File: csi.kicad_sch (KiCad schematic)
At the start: 40 parts, among them J15 Bus_DDR4_SODIMM_CUSTOM_Jetson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, T8 BSS138PW, U10 TPS7A0528PDBVR, U11 TLV75512PDBVR, U4 PCA9547_VQFN

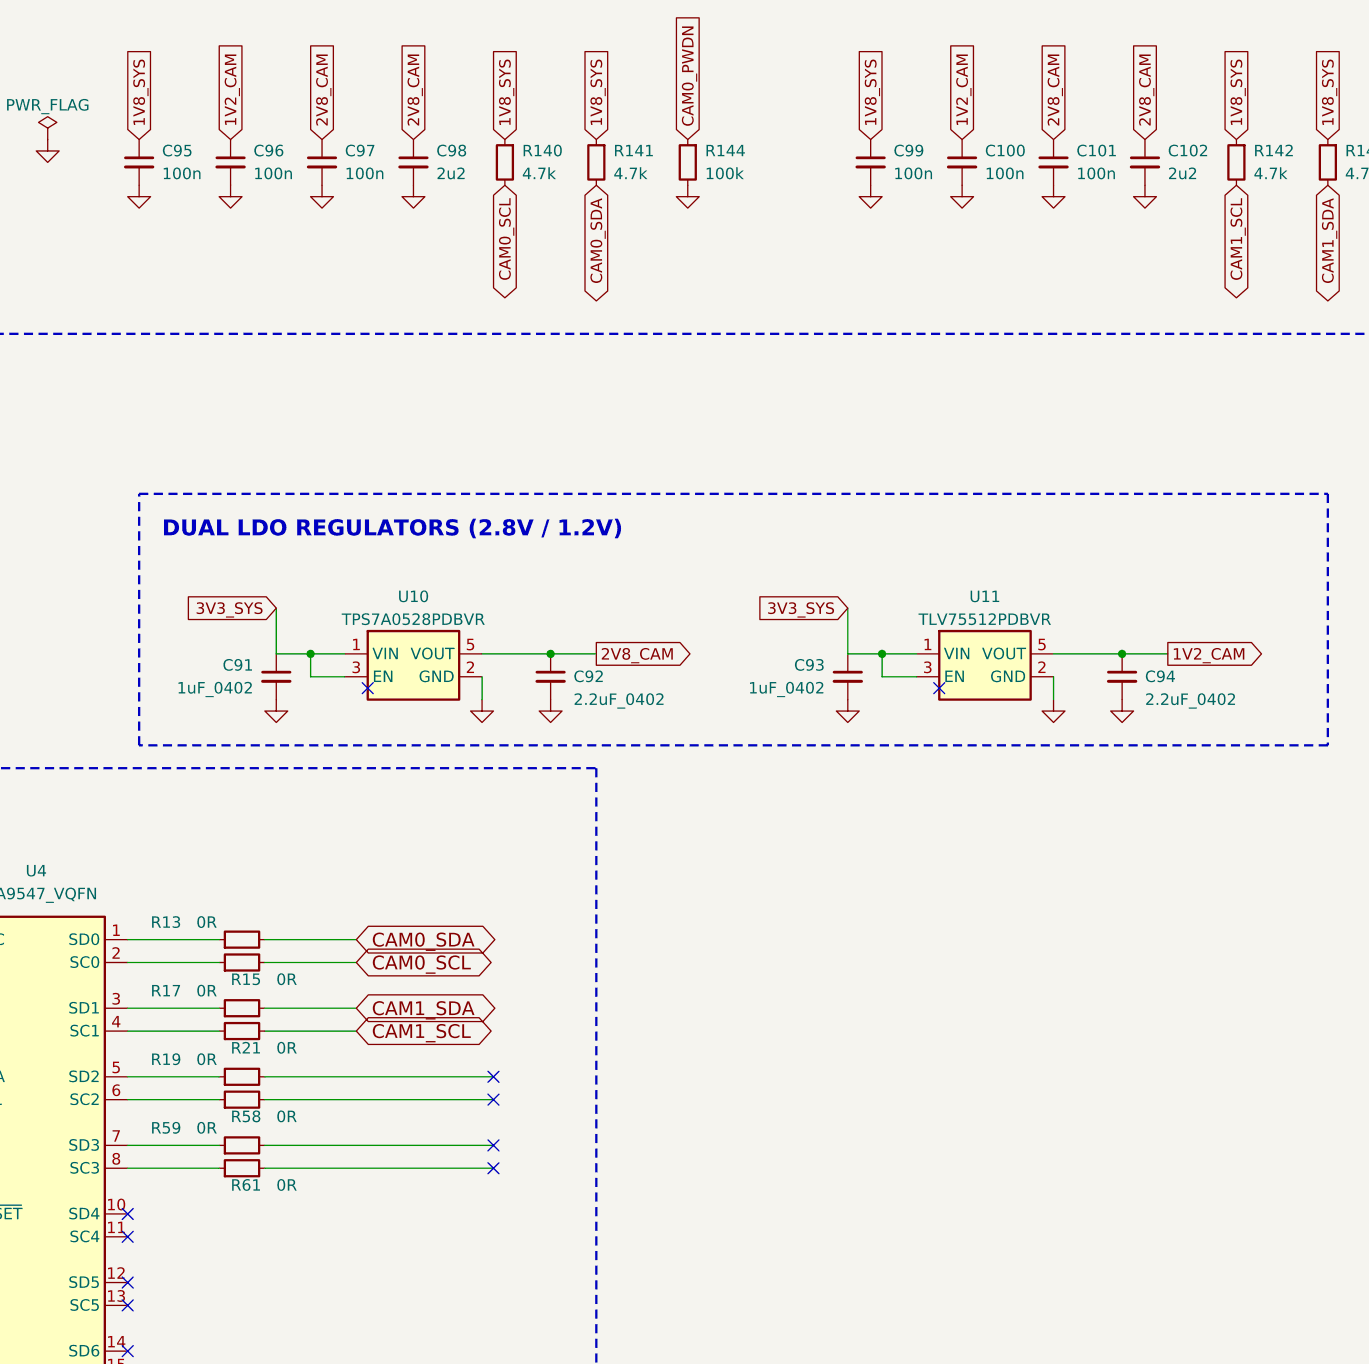
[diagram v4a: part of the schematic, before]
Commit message: fix(sch): resolve all symbol, label, and property collisions on SoM sheet (Page 4)
Flip J10 PCIe global labels outward, stagger C103/C104 and move properties out of wire bundle, shift R112 to clear USR1 value text, hide internal pin text on BSS138PW and BAT1, stagger SP1-SP6 spacer labels, align J15A/J15C/J15F labels, and preserve 100% PCB schematic parity.

Co-Authored-By: CopperPilot <noreply@copperpilot.ai>
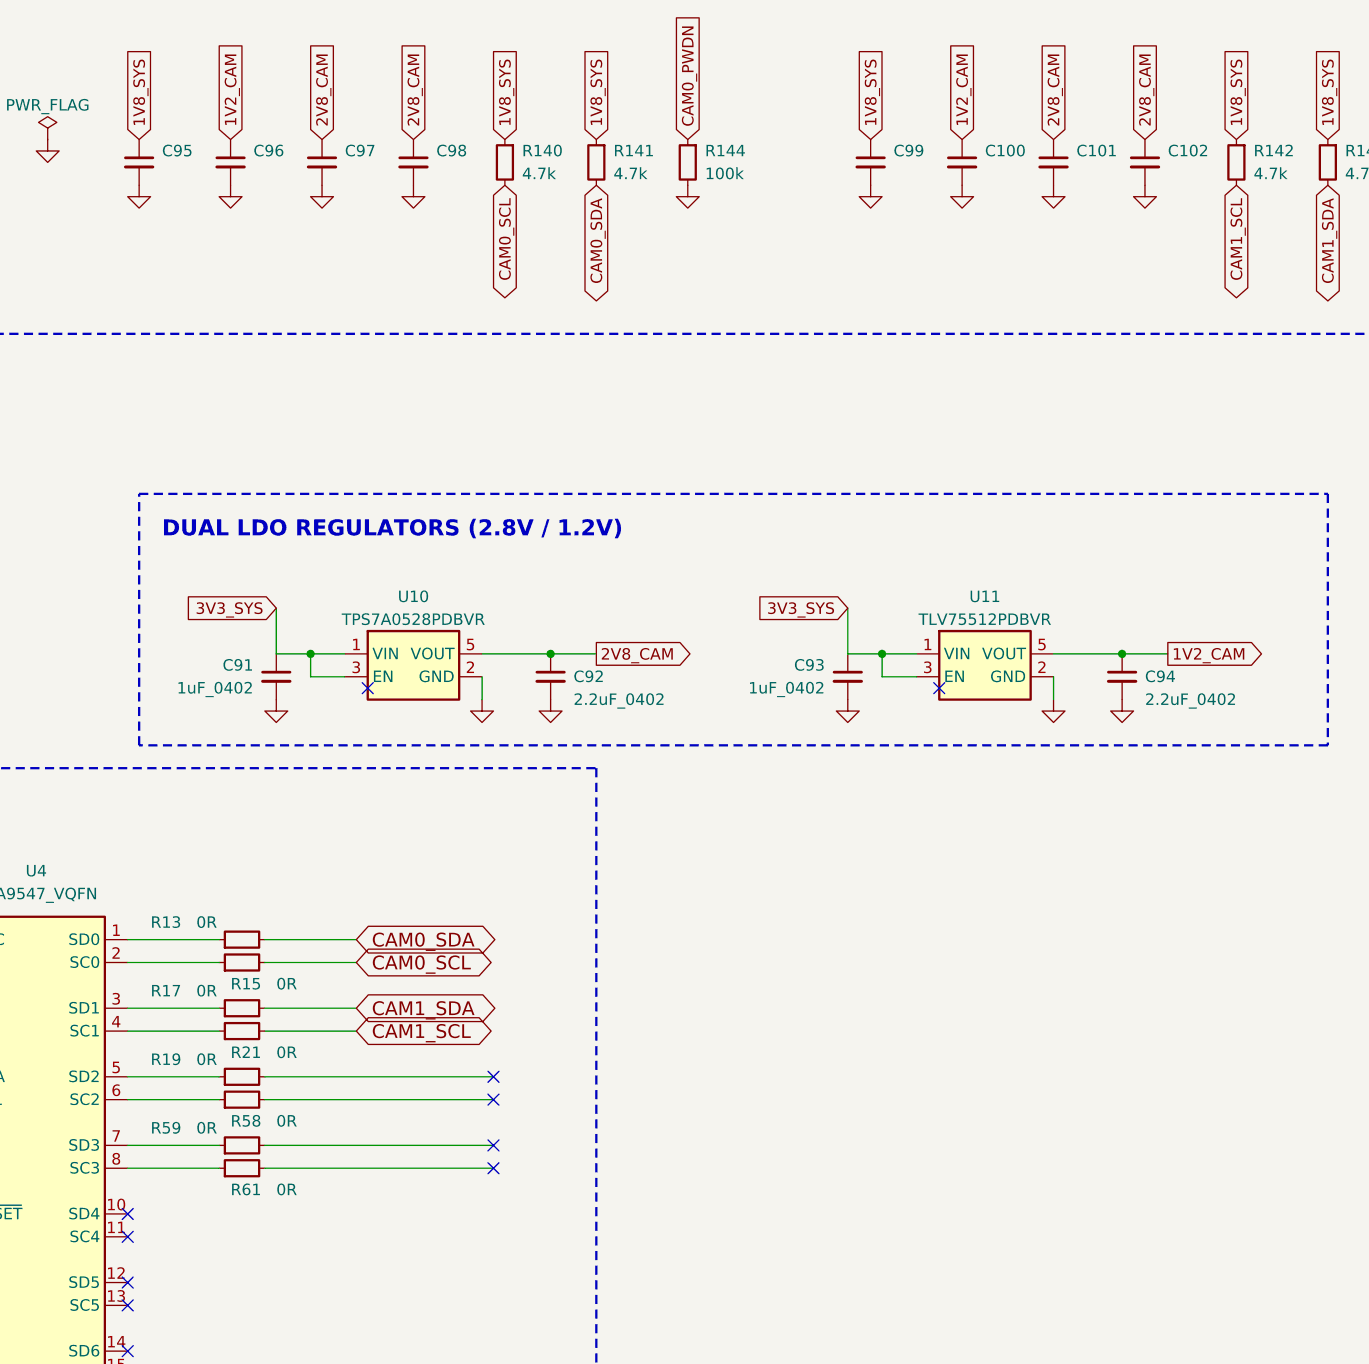
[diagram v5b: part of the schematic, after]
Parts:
- C100, C101, C95, C96, C97, C99: value 100n -> C_100n_0402
- C102, C98: value 2u2 -> C_2u2_0402

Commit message: fix(bom): update LCSC procurement part numbers and SMT assembly flags
Reconcile LCSC part numbers with physical land patterns and active stock:
- J11 USB-C: C456013 (24-pin SuperSpeed receptacle matching Wurth 632723300011)
- J15 SODIMM: C2766246 (TE 2309413-1 260-pin socket)
- J2 Mini-DP: C574827 (TE 2129320-3)
- J1 Micro-HDMI: C563878 (Molex 467651001)
- J5, J9 Micro-USB: C132560 (Molex 473460001)
- REC1, RST1, USR1: C2886925 (E-Switch TL3340AF160QG)
- BAT1: set DNP for SMT reflow to prevent thermal rupture in 260C oven

Co-Authored-By: CopperPilot <noreply@copperpilot.ai>
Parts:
- J15: LCSC C429199 -> C2766246
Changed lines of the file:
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@@
 			)
 		)
-		(property "LCSC" "C429199"
+		(property "LCSC" "C2766246"
 			(at 0 0 0)
 			(effects
